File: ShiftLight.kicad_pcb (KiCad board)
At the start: 2 copper layers, 66.3 x 15.2 mm, 58 parts, among them J1 0533980471, J2 0533980571, U1 VOS618A, U2 LMR51406YDBV, U3 MSPM0C1104SDDFR, U4 TLC59208F, U5 VEML7700, U6 TLV803E

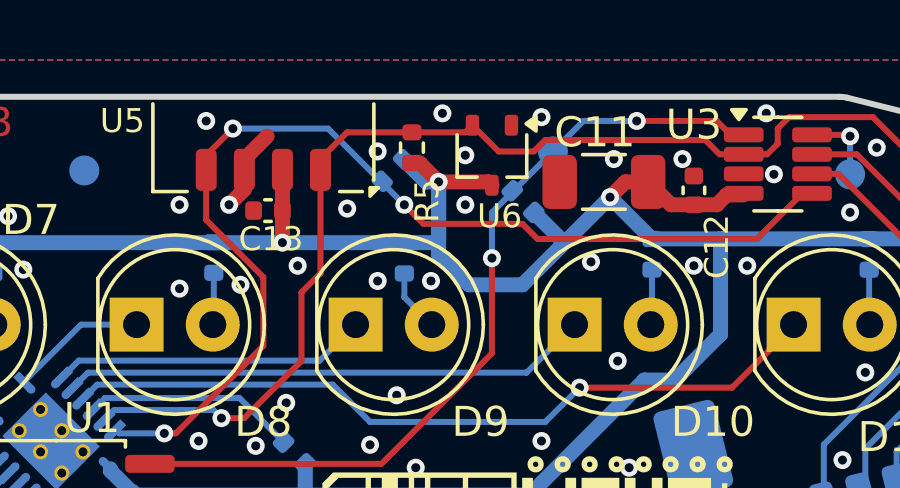
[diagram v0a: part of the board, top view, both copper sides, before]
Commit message: Fix footprint of tlv803e
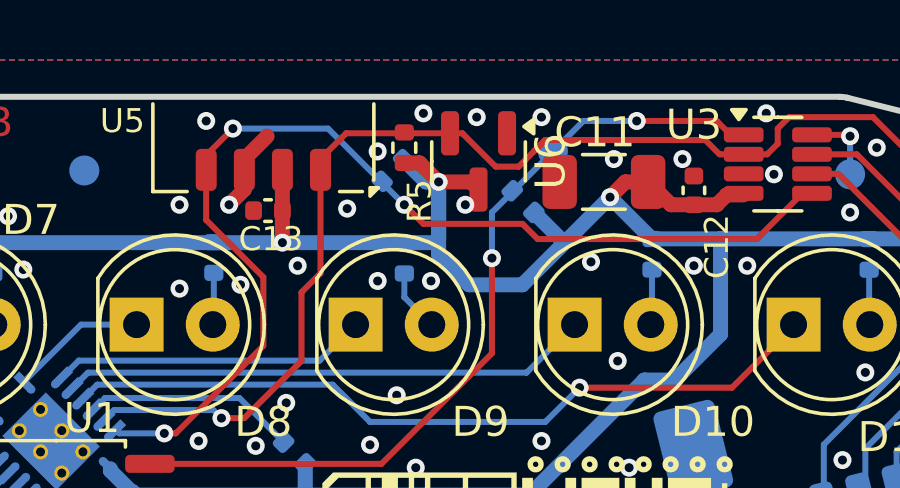
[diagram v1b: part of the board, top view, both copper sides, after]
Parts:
- U6: footprint Package_TO_SOT_SMD:SOT-323_SC-70 -> Package_TO_SOT_SMD:SOT-23
- moved U6 0.49 mm to (123.1, 78.3)
- moved R5 0.25 mm to (120.7, 77.9)
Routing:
- net /02_MCU/I2C_SCL: track 51.9 -> 52.6 mm
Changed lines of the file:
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@@
 	(net 37 "Net-(U3-PA24{slash}A3)")
 	(net 38 "Net-(J1-Pin_1)")
-	(footprint "Package_TO_SOT_SMD:SOT-323_SC-70"
+	(footprint "Package_TO_SOT_SMD:SOT-23"
 		(layer "F.Cu")
-		(at 123.571 78.105 -90)
-		(descr "SOT-323, SC-70")
-		(tags "SOT-323 SC-70")
+		(at 123.124 78.3105 -90)
+		(descr "SOT, 3 Pin (JEDEC TO-236 Var AB https://www.jedec.org/document_search?search_api_views_fulltext=TO-236), generated with kicad-footprint-generator ipc_gullwing_generator.py")
+		(tags "SOT TO_SOT_SMD")
 		(property "Reference" "U6"
-			(at 2.032 -0.254 0)
+			(at 0 -2.4 -90)
 			(layer "F.SilkS")
 			(effects
 				(font
-					(size 0.8 0.8)
+					(size 1 1)
 					(thickness 0.15)
 				)
@@
 		)
 		(property "Value" "TLV803E"
-			(at 1.143 0 180)
+			(at 0 2.4 -90)
 			(layer "F.Fab")
 			(effects
 				(font
-					(size 0.5 0.5)
-					(thickness 0.1)
+					(size 1 1)
+					(thickness 0.15)
 				)
 			)
 		)
-		(property "Footprint" "Package_TO_SOT_SMD:SOT-323_SC-70"
+		(property "Footprint" "Package_TO_SOT_SMD:SOT-23"
 			(at 0 0 -90)
-			(unlocked yes)
 			(layer "F.Fab")
 			(hide yes)
@@
 		(property "Datasheet" ""
 			(at 0 0 -90)
-			(unlocked yes)
 			(layer "F.Fab")
 			(hide yes)
@@
 			)
 		)
-		(property "Description" "Microprocessor Reset (active-low) Circuit, SOT-323"
+		(property "Description" "Microprocessor Reset (active-low) Circuit, SOT-23"
 			(at 0 0 -90)
-			(unlocked yes)
 			(layer "F.Fab")
 			(hide yes)
@@
 		(attr smd)
 		(fp_line
-			(start -0.68 1.16)
-			(end 0.73 1.16)
+			(start 0 1.56)
+			(end -0.65 1.56)
 			(stroke
 				(width 0.12)
@@
 		)
 		(fp_line
-			(start 0.73 0.5)
-			(end 0.73 1.16)
+			(start 0 1.56)
+			(end 0.65 1.56)
 			(stroke
 				(width 0.12)
@@
 		)
 		(fp_line
-			(start -0.68 -1.16)
-			(end 0.73 -1.16)
+			(start 0 -1.56)
+			(end -0.65 -1.56)
 			(stroke
 				(width 0.12)
@@
 		)
 		(fp_line
-			(start 0.73 -1.16)
-			(end 0.73 -0.5)
+			(start 0 -1.56)
+			(end 0.65 -1.56)
 			(stroke
 				(width 0.12)
@@
 		(fp_poly
 			(pts
-				(xy -1.05 -1.14) (xy -1.29 -1.47) (xy -0.81 -1.47) (xy -1.05 -1.14)
+				(xy -1.1625 -1.51) (xy -1.4025 -1.84) (xy -0.9225 -1.84) (xy -1.1625 -1.51)
 			)
 			(stroke
@@
 		)
 		(fp_line
-			(start -1.7 1.3)
-			(end -1.7 -1.3)
+			(start -1.92 1.7)
+			(end 1.92 1.7)
 			(stroke
 				(width 0.05)
@@
 		)
 		(fp_line
-			(start 1.7 1.3)
-			(end -1.7 1.3)
+			(start 1.92 1.7)
+			(end 1.92 -1.7)
 			(stroke
 				(width 0.05)
@@
 		)
 		(fp_line
-			(start -1.7 -1.3)
-			(end 1.7 -1.3)
+			(start -1.92 -1.7)
+			(end -1.92 1.7)
 			(stroke
 				(width 0.05)
@@
 		)
 		(fp_line
-			(start 1.7 -1.3)
-			(end 1.7 1.3)
+			(start 1.92 -1.7)
+			(end -1.92 -1.7)
 			(stroke
 				(width 0.05)
@@
 		)
 		(fp_line
-			(start 0.67 1.1)
-			(end -0.68 1.1)
+			(start -0.65 1.45)
+			(end -0.65 -1.125)
 			(stroke
 				(width 0.1)
@@
 		)
 		(fp_line
-			(start -0.68 -0.6)
-			(end -0.68 1.1)
+			(start 0.65 1.45)
+			(end -0.65 1.45)
 			(stroke
 				(width 0.1)
@@
 		)
 		(fp_line
-			(start -0.18 -1.1)
-			(end -0.68 -0.6)
+			(start -0.65 -1.125)
+			(end -0.325 -1.45)
 			(stroke
 				(width 0.1)
@@
 		)
 		(fp_line
-			(start 0.67 -1.1)
-			(end 0.67 1.1)
+			(start -0.325 -1.45)
+			(end 0.65 -1.45)
 			(stroke
 				(width 0.1)
@@
 		)
 		(fp_line
-			(start 0.67 -1.1)
-			(end -0.18 -1.1)
+			(start 0.65 -1.45)
+			(end 0.65 1.45)
 			(stroke
 				(width 0.1)
@@
 		)
 		(fp_text user "${REFERENCE}"
-			(at 0 0 0)
+			(at 0 0 -90)
 			(layer "F.Fab")
 			(effects
 				(font
-					(size 0.5 0.5)
-					(thickness 0.075)
+					(size 0.32 0.32)
+					(thickness 0.05)
 				)
 			)
 		)
 		(pad "1" smd roundrect
-			(at -1 -0.65 180)
-			(size 0.45 0.7)
+			(at -0.9375 -0.95 270)
+			(size 1.475 0.6)
 			(layers "F.Cu" "F.Paste" "F.Mask")
 			(roundrect_rratio 0.25)
@@
 		)
 		(pad "2" smd roundrect
-			(at -1 0.65 180)
-			(size 0.45 0.7)
+			(at -0.9375 0.95 270)
+			(size 1.475 0.6)
 			(layers "F.Cu" "F.Paste" "F.Mask")
 			(roundrect_rratio 0.25)
@@
 		)
 		(pad "3" smd roundrect
-			(at 1 0 180)
-			(size 0.45 0.7)
+			(at 0.9375 0 270)
+			(size 1.475 0.6)
 			(layers "F.Cu" "F.Paste" "F.Mask")
 			(roundrect_rratio 0.25)
@@
 			(pintype "power_in")
 		)
-		(model "${KICAD8_3DMODEL_DIR}/Package_TO_SOT_SMD.3dshapes/SOT-323_SC-70.wrl"
+		(model "${KICAD8_3DMODEL_DIR}/Package_TO_SOT_SMD.3dshapes/SOT-23.wrl"
 			(offset
 				(xyz 0 0 0)
@@
 	(footprint "Resistor_SMD:R_0402_1005Metric"
 		(layer "F.Cu")
-		(at 120.904 77.851 90)
+		(at 120.65 77.852999 90)
 		(descr "Resistor SMD 0402 (1005 Metric), square (rectangular) end terminal, IPC_7351 nominal, (Body size source: IPC-SM-782 page 72, https://www.pcb-3d.com/wordpress/wp-content/uploads/ipc-sm-782a_amendment_1_and_2.pdf), generated with kicad-footprint-generator")
 		(tags "resistor")
@@
 	)
 	(segment
-		(start 121.793 78.994)
-		(end 123.46 78.994)
+		(start 121.159999 78.360999)
+		(end 120.65 78.360999)
+		(width 0.5)
+		(layer "F.Cu")
+		(net 2)
+	)
+	(segment
+		(start 122.87 78.994)
+		(end 123.124 79.248)
 		(width 0.5)
 		(layer "F.Cu")
@@
 	)
 	(segment
-		(start 121.793 78.994)
-		(end 121.159999 78.360999)
-		(width 0.5)
-		(layer "F.Cu")
-		(net 2)
-	)
-	(segment
 		(start 116.586 79.949602)
 		(end 116.586 78.592602)
@@
 	)
 	(segment
-		(start 121.159999 78.360999)
-		(end 120.904 78.360999)
-		(width 0.5)
-		(layer "F.Cu")
-		(net 2)
-	)
-	(segment
 		(start 128.016 78.994)
 		(end 127.508 79.502)
@@
 	)
 	(segment
-		(start 123.46 78.994)
-		(end 123.571 79.105)
+		(start 128.778 78.994)
+		(end 129.54 79.756)
 		(width 0.5)
 		(layer "F.Cu")
@@
 	)
 	(segment
-		(start 128.778 78.994)
-		(end 129.54 79.756)
+		(start 141.605 84.952)
+		(end 141.605 84.328)
 		(width 0.5)
 		(layer "F.Cu")
@@
 	)
 	(segment
-		(start 141.605 84.952)
-		(end 141.605 84.328)
+		(start 121.793 78.994)
+		(end 121.159999 78.360999)
 		(width 0.5)
 		(layer "F.Cu")
@@
 		(net 2)
 	)
+	(segment
+		(start 121.793 78.994)
+		(end 122.87 78.994)
+		(width 0.5)
+		(layer "F.Cu")
+		(net 2)
+	)
 	(via
 		(at 127.508 79.502)
@@
 	)
 	(via
-		(at 121.92 76.708)
+		(at 123.063 76.835)
 		(size 0.6)
 		(drill 0.3)
@@
 	)
 	(via
-		(at 122.682 78.105)
+		(at 87.884 79.121)
 		(size 0.6)
 		(drill 0.3)
@@
 	)
 	(via
-		(at 87.884 79.121)
+		(at 135.255 88.265)
 		(size 0.6)
 		(drill 0.3)
@@
 	)
 	(via
-		(at 135.255 88.265)
+		(at 121.285 76.708)
 		(size 0.6)
 		(drill 0.3)
@@
 	)
 	(segment
-		(start 140.335 86.36)
-		(end 140.335 84.455)
+		(start 124.46 78.486)
+		(end 123.698 78.486)
 		(width 0.2)
 		(layer "F.Cu")
@@
 	)
 	(segment
-		(start 132.745 78.075)
-		(end 131.964 78.075)
+		(start 140.335 86.36)
+		(end 140.335 84.455)
 		(width 0.2)
 		(layer "F.Cu")
@@
 	)
 	(segment
-		(start 123.794 77.978)
-		(end 124.968 77.978)
+		(start 132.745 78.075)
+		(end 131.964 78.075)
 		(width 0.2)
 		(layer "F.Cu")
@@
 	)
 	(segment
-		(start 122.684999 77.341001)
-		(end 118.741899 77.341001)
+		(start 131.161 78.075)
+		(end 131.964 78.075)
 		(width 0.2)
 		(layer "F.Cu")
@@
 	)
 	(segment
-		(start 131.161 78.075)
-		(end 131.964 78.075)
+		(start 117.856 78.2269)
+		(end 117.856 78.592602)
 		(width 0.2)
 		(layer "F.Cu")
@@
 	)
 	(segment
-		(start 117.856 78.2269)
+		(start 117.856 82.042)
 		(end 117.856 78.592602)
 		(width 0.2)
@@
 	)
 	(segment
-		(start 117.856 82.042)
-		(end 117.856 78.592602)
+		(start 125.349 77.597)
+		(end 124.46 78.486)
 		(width 0.2)
 		(layer "F.Cu")
@@
 	)
 	(segment
-		(start 122.921 77.105)
-		(end 123.794 77.978)
+		(start 122.585 77.373)
+		(end 122.174 77.373)
 		(width 0.2)
 		(layer "F.Cu")
@@
 	)
 	(segment
-		(start 122.921 77.105)
-		(end 122.684999 77.341001)
+		(start 117.221 84.963)
+		(end 117.221 82.677)
 		(width 0.2)
 		(layer "F.Cu")
@@
 	)
 	(segment
-		(start 117.221 84.963)
-		(end 117.221 82.677)
+		(start 123.698 78.486)
+		(end 122.585 77.373)
+		(width 0.2)
+		(layer "F.Cu")
+		(net 4)
+	)
+	(segment
+		(start 122.174 77.373)
+		(end 118.7099 77.373)
 		(width 0.2)
 		(layer "F.Cu")
@@
 	)
 	(segment
-		(start 118.741899 77.341001)
+		(start 118.7099 77.373)
 		(end 117.856 78.2269)
 		(width 0.2)

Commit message: cleanup silkscreen
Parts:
- moved R5 3.49 mm to (124.1, 78.5)
- moved U6 1.71 mm to (121.4, 78.3)
- moved R6 0.18 mm to (120.4, 78.5), turned to 180 degrees
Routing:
- net 3V3: track 129.3 -> 127.9 mm
- net /02_MCU/I2C_SDA: track 36.0 -> 36.6 mm
- net /02_MCU/I2C_SCL: track 52.6 -> 52.1 mm
- net GND: vias 84 -> 83
